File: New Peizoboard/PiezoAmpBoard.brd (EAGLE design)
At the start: 75 x 56.6 mm, 89 parts, among them IC3 TL072D, IC5 TL072D, IC6 TL072D, IC7 TL072D, U1 ARDUINOR3-BPLACE, U2 MIC5219 3.3V, X1 22-23-2021, X2 22-23-2021

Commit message: add 9v and 3v indicator LEDs
From mac
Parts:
- added D1, D2: (no value), SparkFun-LED:LED-0603
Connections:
- new net N$1: D1.A, R5.1
- new net N$2: D2.A, R6.1
- net GND: now also D1.C, D2.C
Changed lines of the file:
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@@
 <element name="R5" library="rcl" package="R0603" value="" x="-17.78" y="-127"/>
 <element name="R6" library="rcl" package="R0603" value="" x="-17.78" y="-130.81"/>
+<element name="D1" library="SparkFun-LED" package="LED-0603" value="" x="-21.59" y="-129.54"/>
+<element name="D2" library="SparkFun-LED" package="LED-0603" value="" x="-25.4" y="-129.54"/>
 </elements>
 <signals>
@@
 <contactref element="C3" pad="1"/>
 <contactref element="C2" pad="2"/>
+<contactref element="D1" pad="C"/>
+<contactref element="D2" pad="C"/>
+<wire x1="-21.59" y1="-128.663" x2="-25.4" y2="-128.663" width="0" layer="19" extent="1-1"/>
+<wire x1="-18.63" y1="-121.92" x2="-21.59" y2="-128.663" width="0" layer="19" extent="1-1"/>
 <wire x1="-18.63" y1="-116.84" x2="-18.63" y2="-121.92" width="0" layer="19" extent="1-1"/>
 <wire x1="-17.78" y1="-113.0601" x2="-18.63" y2="-116.84" width="0" layer="19" extent="1-1"/>
@@
 <wire x1="-18.73" y1="-113.0601" x2="-16.83" y2="-113.0601" width="0" layer="19" extent="1-1"/>
 </signal>
+<signal name="N$1">
+<contactref element="R5" pad="1"/>
+<contactref element="D1" pad="A"/>
+<wire x1="-18.63" y1="-127" x2="-21.59" y2="-130.417" width="0" layer="19" extent="1-1"/>
+</signal>
+<signal name="N$2">
+<contactref element="R6" pad="1"/>
+<contactref element="D2" pad="A"/>
+<wire x1="-18.63" y1="-130.81" x2="-25.4" y2="-130.417" width="0" layer="19" extent="1-1"/>
+</signal>
 </signals>

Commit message: add 3 teensy indicator LEDs
from pc
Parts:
- added D3, D4, D5: (no value), SparkFun-LED:LED-0603
- added R7, R8, R9: (no value), rcl:R0603
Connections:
- new net N$3: D3.A, U$2.3
- new net N$4: D4.A, U$2.4
- new net N$5: D5.A, U$2.5
- new net N$6: D3.C, R9.2
- new net N$7: D4.C, R8.2
- new net N$8: D5.C, R7.2
- net GND: now also R7.1, R8.1, R9.1
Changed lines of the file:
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@@
 <?xml version="1.0" encoding="utf-8"?>
 <!DOCTYPE eagle SYSTEM "eagle.dtd">
-<eagle version="7.4.0">
+<eagle version="8.0.2">
 <drawing>
 <settings>
@@
 <element name="U1" library="adafruit" package="ARDUINOR3-BPLACE" value="ARDUINOR3-BPLACE" x="10.972375" y="2.54"/>
 <element name="X1" library="con-molex" package="22-23-2021" value="22-23-2021" x="74.22489375" y="13.63450625" rot="R90">
+<attribute name="MF" value="MOLEX" x="74.22489375" y="13.63450625" size="1.778" layer="27" rot="R90" display="off"/>
 <attribute name="MPN" value="22-23-2021" x="74.22489375" y="13.63450625" size="1.778" layer="27" rot="R90" display="off"/>
-<attribute name="MF" value="MOLEX" x="74.22489375" y="13.63450625" size="1.778" layer="27" rot="R90" display="off"/>
+<attribute name="OC_FARNELL" value="1462926" x="74.22489375" y="13.63450625" size="1.778" layer="27" rot="R90" display="off"/>
 <attribute name="OC_NEWARK" value="25C3832" x="74.22489375" y="13.63450625" size="1.778" layer="27" rot="R90" display="off"/>
-<attribute name="OC_FARNELL" value="1462926" x="74.22489375" y="13.63450625" size="1.778" layer="27" rot="R90" display="off"/>
 </element>
 <element name="X2" library="con-molex" package="22-23-2021" value="22-23-2021" x="73.171634375" y="46.317578125" rot="R90">
+<attribute name="MF" value="MOLEX" x="73.171634375" y="46.317578125" size="1.778" layer="27" rot="R90" display="off"/>
 <attribute name="MPN" value="22-23-2021" x="73.171634375" y="46.317578125" size="1.778" layer="27" rot="R90" display="off"/>
-<attribute name="MF" value="MOLEX" x="73.171634375" y="46.317578125" size="1.778" layer="27" rot="R90" display="off"/>
+<attribute name="OC_FARNELL" value="1462926" x="73.171634375" y="46.317578125" size="1.778" layer="27" rot="R90" display="off"/>
 <attribute name="OC_NEWARK" value="25C3832" x="73.171634375" y="46.317578125" size="1.778" layer="27" rot="R90" display="off"/>
-<attribute name="OC_FARNELL" value="1462926" x="73.171634375" y="46.317578125" size="1.778" layer="27" rot="R90" display="off"/>
 </element>
 <element name="U$6" library="BAV99T" package="SOT-523" value="BAV99T" x="62.77190625" y="8.385715625" rot="R90"/>
 <element name="C28" library="eagle-ltspice" package="C0603" value=".1uF" x="59.526221875" y="10.6775875" rot="R180">
+<attribute name="SPICEMODEL" value="NONE" x="59.526221875" y="10.6775875" size="1.778" layer="27" rot="R180" display="off"/>
 <attribute name="SPICEPREFIX" value="C" x="59.526221875" y="10.6775875" size="1.778" layer="27" rot="R180" display="off"/>
-<attribute name="SPICEMODEL" value="NONE" x="59.526221875" y="10.6775875" size="1.778" layer="27" rot="R180" display="off"/>
 </element>
 <element name="U$11" library="3mmJack" package="1X05" value="3MMJACK" x="6.562040625" y="14.436203125"/>
@@
 <element name="D1" library="SparkFun-LED" package="LED-0603" value="" x="-21.59" y="-129.54"/>
 <element name="D2" library="SparkFun-LED" package="LED-0603" value="" x="-25.4" y="-129.54"/>
+<element name="D3" library="SparkFun-LED" package="LED-0603" value="" x="-25.4" y="-134.62"/>
+<element name="D4" library="SparkFun-LED" package="LED-0603" value="" x="-25.4" y="-138.43"/>
+<element name="D5" library="SparkFun-LED" package="LED-0603" value="" x="-25.4" y="-142.24"/>
+<element name="R7" library="rcl" package="R0603" value="" x="-25.4" y="-146.05"/>
+<element name="R8" library="rcl" package="R0603" value="" x="-25.4" y="-151.13"/>
+<element name="R9" library="rcl" package="R0603" value="" x="-25.4" y="-156.21"/>
 </elements>
 <signals>
@@
 <contactref element="D1" pad="C"/>
 <contactref element="D2" pad="C"/>
+<contactref element="R9" pad="1"/>
+<contactref element="R7" pad="1"/>
+<contactref element="R8" pad="1"/>
+<wire x1="-26.25" y1="-151.13" x2="-26.25" y2="-156.21" width="0" layer="19" extent="1-1"/>
+<wire x1="-26.25" y1="-146.05" x2="-26.25" y2="-151.13" width="0" layer="19" extent="1-1"/>
+<wire x1="-25.4" y1="-128.663" x2="-26.25" y2="-146.05" width="0" layer="19" extent="1-1"/>
 <wire x1="-21.59" y1="-128.663" x2="-25.4" y2="-128.663" width="0" layer="19" extent="1-1"/>
 <wire x1="-18.63" y1="-121.92" x2="-21.59" y2="-128.663" width="0" layer="19" extent="1-1"/>
@@
 <wire x1="-18.63" y1="-130.81" x2="-25.4" y2="-130.417" width="0" layer="19" extent="1-1"/>
 </signal>
+<signal name="N$3">
+<contactref element="U$2" pad="3"/>
+<contactref element="D3" pad="A"/>
+<wire x1="-13.97" y1="-60.96" x2="-25.4" y2="-135.497" width="0" layer="19" extent="1-1"/>
+</signal>
+<signal name="N$4">
+<contactref element="U$2" pad="4"/>
+<contactref element="D4" pad="A"/>
+<wire x1="-13.97" y1="-63.5" x2="-25.4" y2="-139.307" width="0" layer="19" extent="1-1"/>
+</signal>
+<signal name="N$5">
+<contactref element="U$2" pad="5"/>
+<contactref element="D5" pad="A"/>
+<wire x1="-13.97" y1="-66.04" x2="-25.4" y2="-143.117" width="0" layer="19" extent="1-1"/>
+</signal>
+<signal name="N$6">
+<contactref element="D3" pad="C"/>
+<contactref element="R9" pad="2"/>
+<wire x1="-25.4" y1="-133.743" x2="-24.55" y2="-156.21" width="0" layer="19" extent="1-1"/>
+</signal>
+<signal name="N$7">
+<contactref element="D4" pad="C"/>
+<contactref element="R8" pad="2"/>
+<wire x1="-25.4" y1="-137.553" x2="-24.55" y2="-151.13" width="0" layer="19" extent="1-1"/>
+</signal>
+<signal name="N$8">
+<contactref element="D5" pad="C"/>
+<contactref element="R7" pad="2"/>
+<wire x1="-25.4" y1="-141.363" x2="-24.55" y2="-146.05" width="0" layer="19" extent="1-1"/>
+</signal>
 </signals>

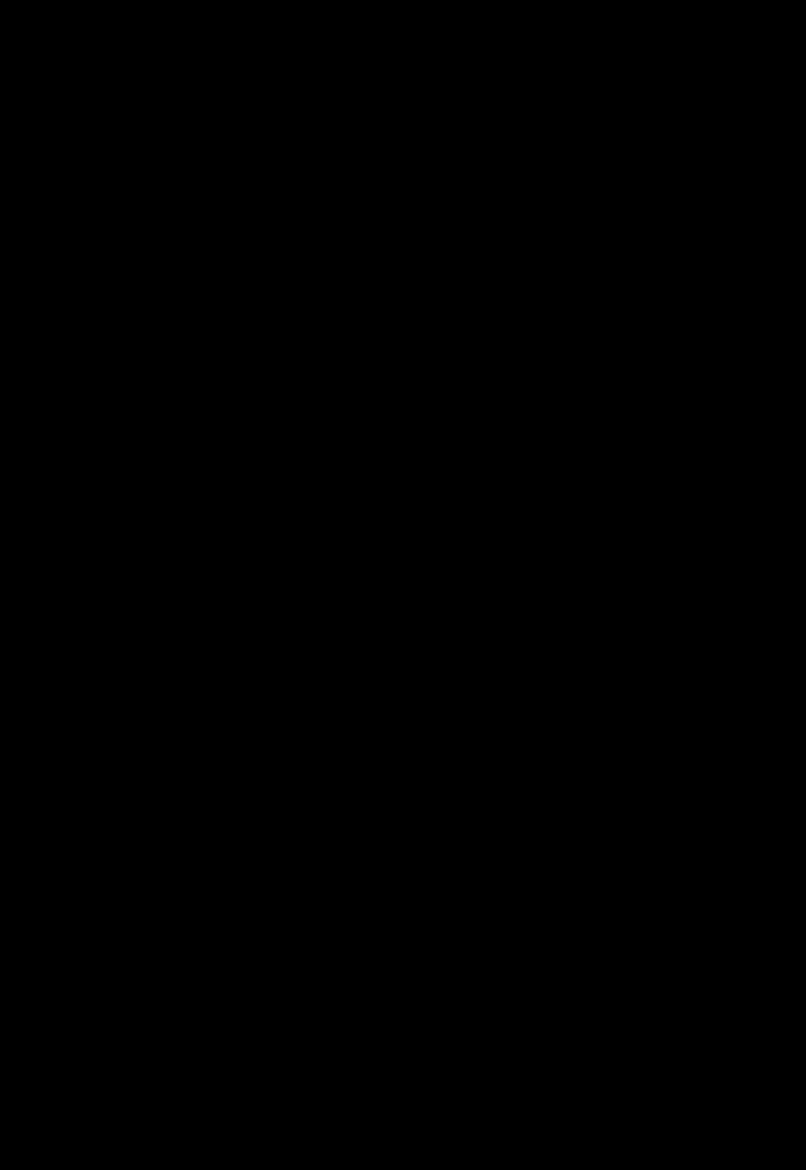
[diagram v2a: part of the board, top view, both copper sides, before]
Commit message: Add all parts, still need some wires, need serial connection
from pc
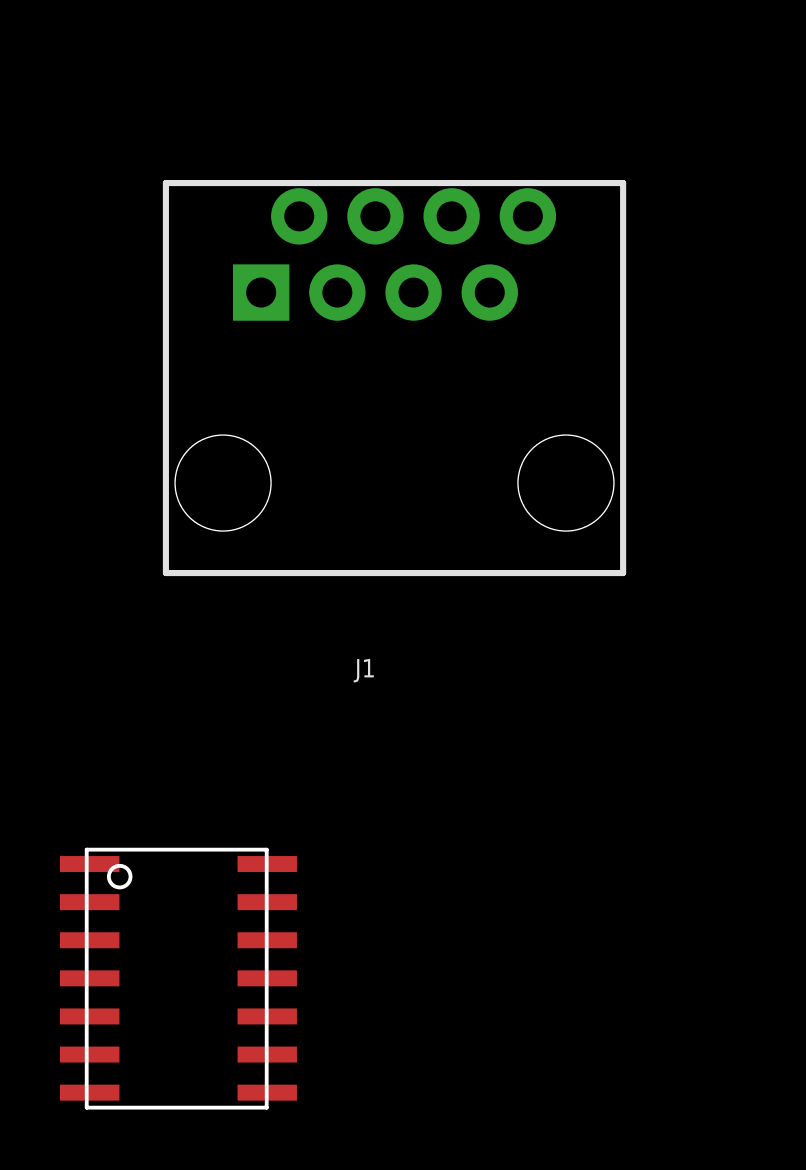
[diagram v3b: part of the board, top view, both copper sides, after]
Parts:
- added J1: RJ45, SparkFun-Connectors:RJ45-8
- added U$3: MAX3491, BackplaneParts:MAX3491
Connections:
- removed net 3V3: U$2.3V3_1
- new net N$10: J1.7, U$3.Z
- new net N$11: J1.6, U$3.B
- new net N$12: J1.5, U$3.A
- new net N$9: J1.8, U$3.Y
- net 3.3V: now also U$2.3V3_1, U$2.3V3_MAX_250, U$3.VCC13, U$3.VCC14
- net GND: now also U$3.GND6, U$3.GND7
- net N$3: now also U$2.38; no longer U$2.3
- net N$4: now also U$2.37; no longer U$2.4
- net N$5: now also U$2.36; no longer U$2.5
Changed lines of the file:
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@@
 <layer number="112" name="tSilk" color="7" fill="1" visible="no" active="yes"/>
 <layer number="113" name="ReferenceLS" color="7" fill="1" visible="no" active="no"/>
+<layer number="114" name="Badge_Outline" color="7" fill="1" visible="yes" active="yes"/>
+<layer number="115" name="ReferenceISLANDS" color="7" fill="1" visible="yes" active="yes"/>
 <layer number="116" name="Patch_BOT" color="9" fill="4" visible="no" active="yes"/>
 <layer number="118" name="Rect_Pads" color="7" fill="1" visible="no" active="no"/>
@@
 <element name="R8" library="rcl" package="R0603" value="" x="-25.4" y="-151.13"/>
 <element name="R9" library="rcl" package="R0603" value="" x="-25.4" y="-156.21"/>
+<element name="J1" library="SparkFun-Connectors" package="RJ45-8" value="RJ45" x="-41.91" y="-146.05">
+<attribute name="PROD_ID" value="CONN-08506" x="-41.91" y="-146.05" size="1.778" layer="27" display="off"/>
+<attribute name="SF_ID" value="PRT-00643" x="-41.91" y="-146.05" size="1.778" layer="27" display="off"/>
+</element>
+<element name="U$3" library="BackplaneParts" package="MAX3491" value="MAX3491" x="-52.07" y="-166.37"/>
 </elements>
 <signals>
@@
 <contactref element="U2" pad="5"/>
 <contactref element="R6" pad="2"/>
+<contactref element="U$3" pad="VCC13"/>
+<contactref element="U$3" pad="VCC14"/>
+<contactref element="U$2" pad="3V3_MAX_250"/>
+<contactref element="U$2" pad="3V3_1"/>
+<wire x1="-46.1515" y1="-158.75" x2="-46.1515" y2="-160.02" width="0" layer="19" extent="1-1"/>
+<wire x1="-16.93" y1="-130.81" x2="-46.1515" y2="-158.75" width="0" layer="19" extent="1-1"/>
 <wire x1="-16.93" y1="-121.92" x2="-16.93" y2="-130.81" width="0" layer="19" extent="1-1"/>
 <wire x1="-18.73" y1="-110.4599" x2="-16.93" y2="-121.92" width="0" layer="19" extent="1-1"/>
-<wire x1="32.967878125" y1="-73.42005625" x2="-18.73" y2="-110.4599" width="0" layer="19" extent="1-1"/>
+<wire x1="-13.97" y1="-86.36" x2="-18.73" y2="-110.4599" width="0" layer="19" extent="1-1"/>
+<wire x1="1.27" y1="-55.88" x2="-13.97" y2="-86.36" width="0" layer="19" extent="1-1"/>
+<wire x1="5.217840625" y1="-31.511496875" x2="1.27" y2="-55.88" width="0" layer="19" extent="1-1"/>
+<wire x1="32.967878125" y1="-73.42005625" x2="1.27" y2="-55.88" width="0" layer="19" extent="1-1"/>
 <wire x1="34.999878125" y1="-73.42005625" x2="32.967878125" y2="-73.42005625" width="0" layer="19" extent="1-1"/>
-<wire x1="5.217840625" y1="-31.511496875" x2="32.967878125" y2="-73.42005625" width="0" layer="19" extent="1-1"/>
 <wire x1="17.787815625" y1="4.859940625" x2="5.217840625" y2="-31.511496875" width="0" layer="19" extent="1-1"/>
 <wire x1="17.787815625" y1="6.759940625" x2="17.787815625" y2="4.859940625" width="0" layer="19" extent="1-1"/>
@@
 <contactref element="R7" pad="1"/>
 <contactref element="R8" pad="1"/>
+<contactref element="U$3" pad="GND6"/>
+<contactref element="U$3" pad="GND7"/>
+<wire x1="-52.07" y1="-166.37" x2="-52.07" y2="-165.1" width="0" layer="19" extent="1-1"/>
+<wire x1="-26.25" y1="-156.21" x2="-52.07" y2="-165.1" width="0" layer="19" extent="1-1"/>
 <wire x1="-26.25" y1="-151.13" x2="-26.25" y2="-156.21" width="0" layer="19" extent="1-1"/>
 <wire x1="-26.25" y1="-146.05" x2="-26.25" y2="-151.13" width="0" layer="19" extent="1-1"/>
@@
 <contactref element="U$2" pad="VIN"/>
 </signal>
-<signal name="3V3">
-<contactref element="U$2" pad="3V3_1"/>
-</signal>
 <signal name="+9V">
 <contactref element="C4" pad="2"/>
@@
 <wire x1="-18.63" y1="-130.81" x2="-25.4" y2="-130.417" width="0" layer="19" extent="1-1"/>
 </signal>
-<signal name="N$3">
-<contactref element="U$2" pad="3"/>
-<contactref element="D3" pad="A"/>
-<wire x1="-13.97" y1="-60.96" x2="-25.4" y2="-135.497" width="0" layer="19" extent="1-1"/>
-</signal>
-<signal name="N$4">
-<contactref element="U$2" pad="4"/>
-<contactref element="D4" pad="A"/>
-<wire x1="-13.97" y1="-63.5" x2="-25.4" y2="-139.307" width="0" layer="19" extent="1-1"/>
-</signal>
-<signal name="N$5">
-<contactref element="U$2" pad="5"/>
-<contactref element="D5" pad="A"/>
-<wire x1="-13.97" y1="-66.04" x2="-25.4" y2="-143.117" width="0" layer="19" extent="1-1"/>
-</signal>
 <signal name="N$6">
 <contactref element="D3" pad="C"/>
@@
 <wire x1="-25.4" y1="-141.363" x2="-24.55" y2="-146.05" width="0" layer="19" extent="1-1"/>
 </signal>
+<signal name="N$3">
+<contactref element="U$2" pad="38"/>
+<contactref element="D3" pad="A"/>
+<wire x1="1.27" y1="-96.52" x2="-25.4" y2="-135.497" width="0" layer="19" extent="1-1"/>
+</signal>
+<signal name="N$4">
+<contactref element="U$2" pad="37"/>
+<contactref element="D4" pad="A"/>
+<wire x1="1.27" y1="-99.06" x2="-25.4" y2="-139.307" width="0" layer="19" extent="1-1"/>
+</signal>
+<signal name="N$5">
+<contactref element="U$2" pad="36"/>
+<contactref element="D5" pad="A"/>
+<wire x1="1.27" y1="-101.6" x2="-25.4" y2="-143.117" width="0" layer="19" extent="1-1"/>
+</signal>
+<signal name="N$9">
+<contactref element="U$3" pad="Y"/>
+<contactref element="J1" pad="8"/>
+<wire x1="-37.465" y1="-137.16" x2="-46.1515" y2="-165.1" width="0" layer="19" extent="1-1"/>
+</signal>
+<signal name="N$10">
+<contactref element="U$3" pad="Z"/>
+<contactref element="J1" pad="7"/>
+<wire x1="-38.735" y1="-139.7" x2="-46.1515" y2="-163.83" width="0" layer="19" extent="1-1"/>
+</signal>
+<signal name="N$11">
+<contactref element="U$3" pad="B"/>
+<contactref element="J1" pad="6"/>
+<wire x1="-40.005" y1="-137.16" x2="-46.1515" y2="-162.56" width="0" layer="19" extent="1-1"/>
+</signal>
+<signal name="N$12">
+<contactref element="U$3" pad="A"/>
+<contactref element="J1" pad="5"/>
+<wire x1="-41.275" y1="-139.7" x2="-46.1515" y2="-161.29" width="0" layer="19" extent="1-1"/>
+</signal>
 </signals>

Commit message: add 2 question points
From PC
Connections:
- net GND5 renamed AGND
- new net RX: U$2.0
- new net SCL: U$2.3
- new net SDA: U$2.4
- new net TX: U$2.1
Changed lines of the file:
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@@
 <wire x1="9.767171875" y1="-45.0788625" x2="8.497171875" y2="-50.2788625" width="0" layer="19" extent="1-1"/>
 </signal>
-<signal name="GND5">
+<signal name="AGND">
 <contactref element="U$1" pad="OUT"/>
 <contactref element="R4" pad="1"/>
@@
 <wire x1="-41.275" y1="-139.7" x2="-46.1515" y2="-161.29" width="0" layer="19" extent="1-1"/>
 </signal>
+<signal name="RX">
+<contactref element="U$2" pad="0"/>
+</signal>
+<signal name="TX">
+<contactref element="U$2" pad="1"/>
+</signal>
+<signal name="SCL">
+<contactref element="U$2" pad="3"/>
+</signal>
+<signal name="SDA">
+<contactref element="U$2" pad="4"/>
+</signal>
 </signals>

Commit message: Compelete the serial connection
From  PC
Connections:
- removed net SCL: U$2.3
- removed net SDA: U$2.4
- new net DE: U$3.DE
- new net RE: U$2.3, U$2.4, U$3.!RE
- net RX: now also U$3.R0
- net TX: now also U$3.DI
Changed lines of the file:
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@@
 <signal name="RX">
 <contactref element="U$2" pad="0"/>
+<contactref element="U$3" pad="R0"/>
+<wire x1="-13.97" y1="-53.34" x2="-52.07" y2="-160.02" width="0" layer="19" extent="1-1"/>
 </signal>
 <signal name="TX">
 <contactref element="U$2" pad="1"/>
+<contactref element="U$3" pad="DI"/>
+<wire x1="-13.97" y1="-55.88" x2="-52.07" y2="-163.83" width="0" layer="19" extent="1-1"/>
 </signal>
-<signal name="SCL">
+<signal name="RE">
+<contactref element="U$3" pad="!RE"/>
 <contactref element="U$2" pad="3"/>
+<contactref element="U$2" pad="4"/>
+<wire x1="-13.97" y1="-63.5" x2="-52.07" y2="-161.29" width="0" layer="19" extent="1-1"/>
+<wire x1="-13.97" y1="-60.96" x2="-13.97" y2="-63.5" width="0" layer="19" extent="1-1"/>
 </signal>
-<signal name="SDA">
-<contactref element="U$2" pad="4"/>
+<signal name="DE">
+<contactref element="U$3" pad="DE"/>
 </signal>
 </signals>
